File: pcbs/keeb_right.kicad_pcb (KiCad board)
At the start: 2 copper layers, 135.3 x 115.9 mm, 70 parts

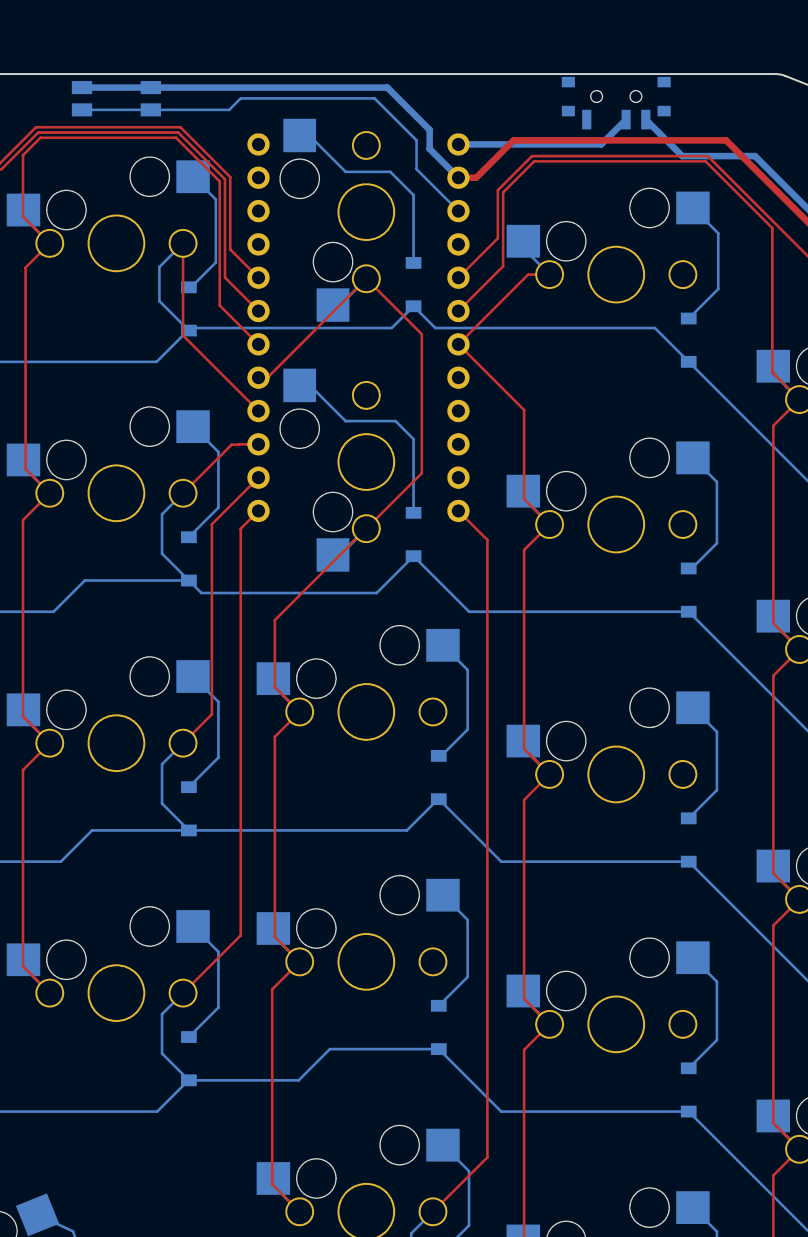
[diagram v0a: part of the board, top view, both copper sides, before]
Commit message: Adding additional outlines for Fusion work, updated MCU placement on PCBs, updated routing to accomodate
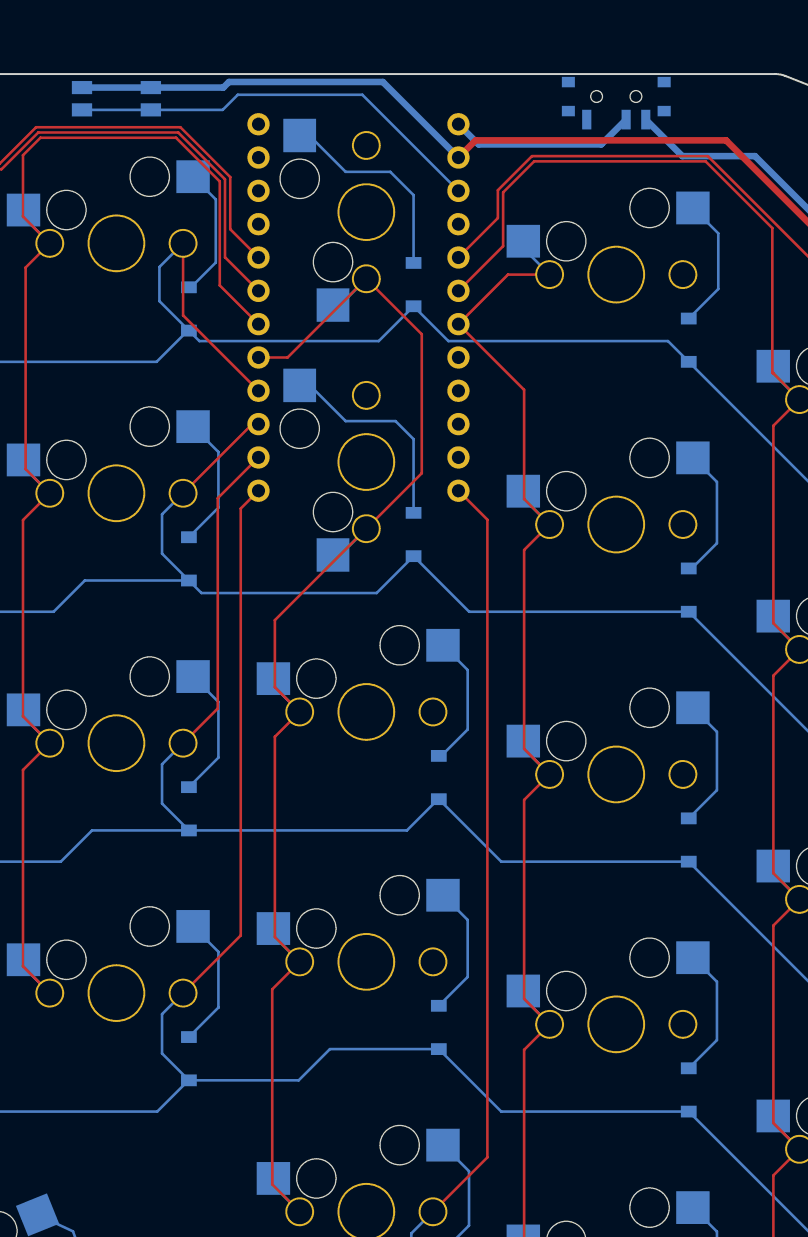
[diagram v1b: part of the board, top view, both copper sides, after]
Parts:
- moved MCU1 1.54 mm to (153.0, 53.3)
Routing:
- net GND: track 75.9 -> 73.5 mm
- net RST: track 33.9 -> 32.2 mm
- net P21: track 161.1 -> 159.5 mm
- net P2: track 172.3 -> 170.7 mm
- net P10: track 180.8 -> 182.3 mm
- net P9: track 150.4 -> 152.0 mm
- net P8: track 156.9 -> 158.5 mm
- net P4: track 113.7 -> 112.1 mm
- net P20: track 147.8 -> 146.3 mm
- net P3: track 161.9 -> 160.4 mm
- net P19: track 104.6 -> 105.5 mm
- net P5: track 109.8 -> 109.2 mm
- net RAW: track 13.6 -> 14.2 mm
- net P7: track 142.0 -> 142.6 mm
- net P6: track 149.2 -> 148.6 mm
